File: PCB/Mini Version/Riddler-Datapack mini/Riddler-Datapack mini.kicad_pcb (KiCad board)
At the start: 4 copper layers, 50 x 68 mm, 57 parts, among them J1 UJ20-C-H-G-SMT-1-P16-TR, J2 DISPLAY, J4 Micro_SD_Card, SW1 RST, SW2 BOOT, U1 USBLC6-2P6, U2 ESP32-S3-MINI-1, U3 TLV62568DBV

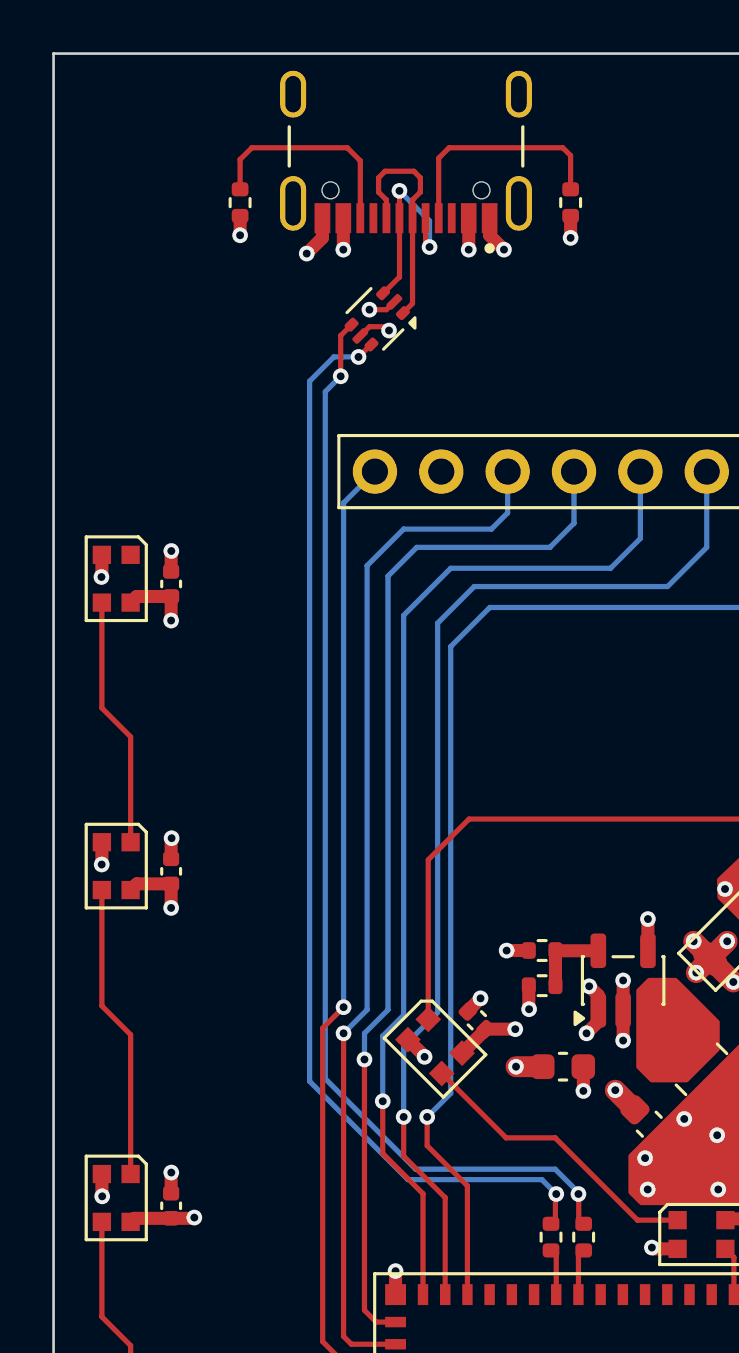
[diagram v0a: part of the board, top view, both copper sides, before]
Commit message: updated usbc location, added more relief vias to vbus and gnd
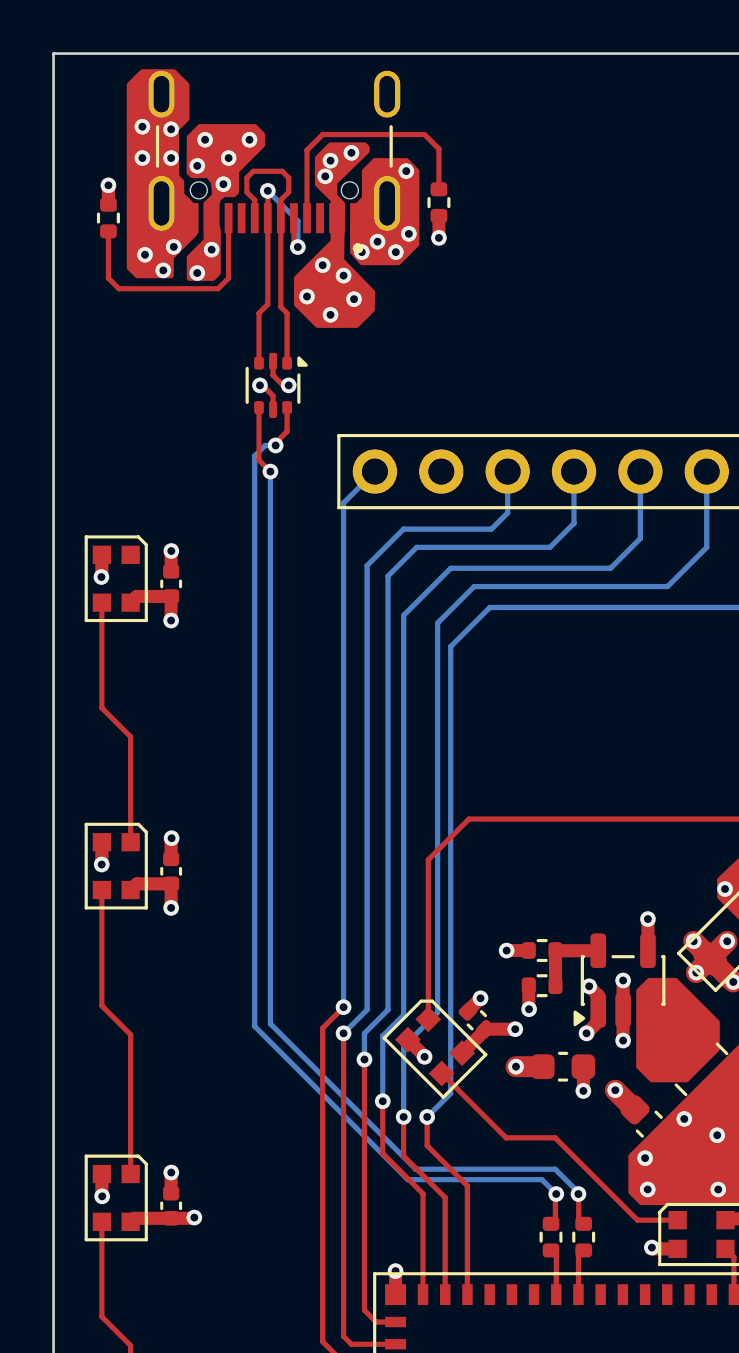
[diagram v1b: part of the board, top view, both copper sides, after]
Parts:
- moved R5 5.07 mm to (52.1, 36.3), turned to 90 degrees
- moved R4 5.04 mm to (64.8, 35.7)
- moved J1 5.04 mm to (58.5, 29.0)
- moved U1 4.73 mm to (58.4, 42.7), turned to -90 degrees
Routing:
- net GND: track 69.8 -> 67.0 mm, vias 70 -> 80
- net /Logic/D-: track 42.2 -> 39.5 mm
- net /Power/U_D-: track 7.97 -> 10.5 mm
- net VBUS: track 3.72 -> 1.19 mm, vias 11 -> 24
- net /Logic/D+: track 42.3 -> 40.0 mm
- net /Power/U_D+: track 8.93 -> 10.8 mm
- net /Power/CC1: track 8.92 -> 9.67 mm
- net /Power/CC2: track 8.33 -> 9.03 mm

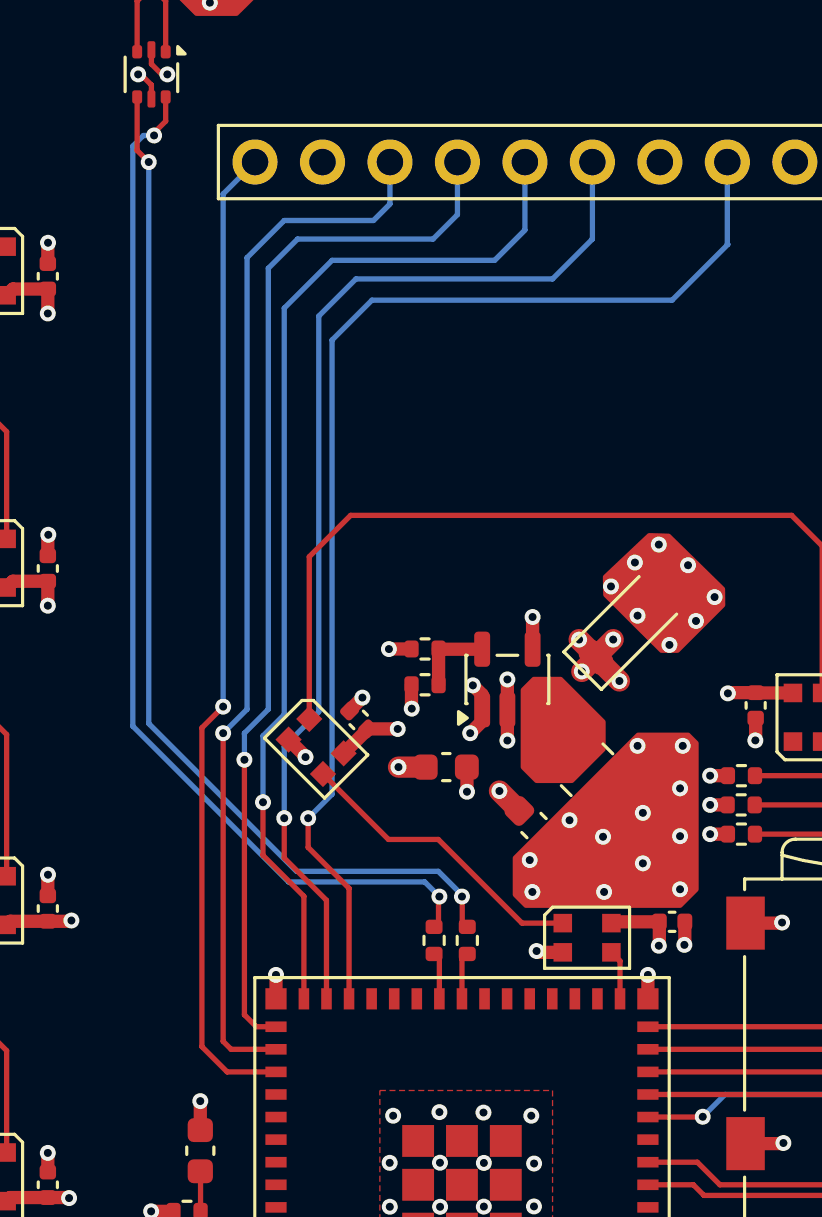
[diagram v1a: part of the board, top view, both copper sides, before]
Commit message: v1.1: update Mini Datapack with repositioned USB-C, relief vias, and v1p1 exports
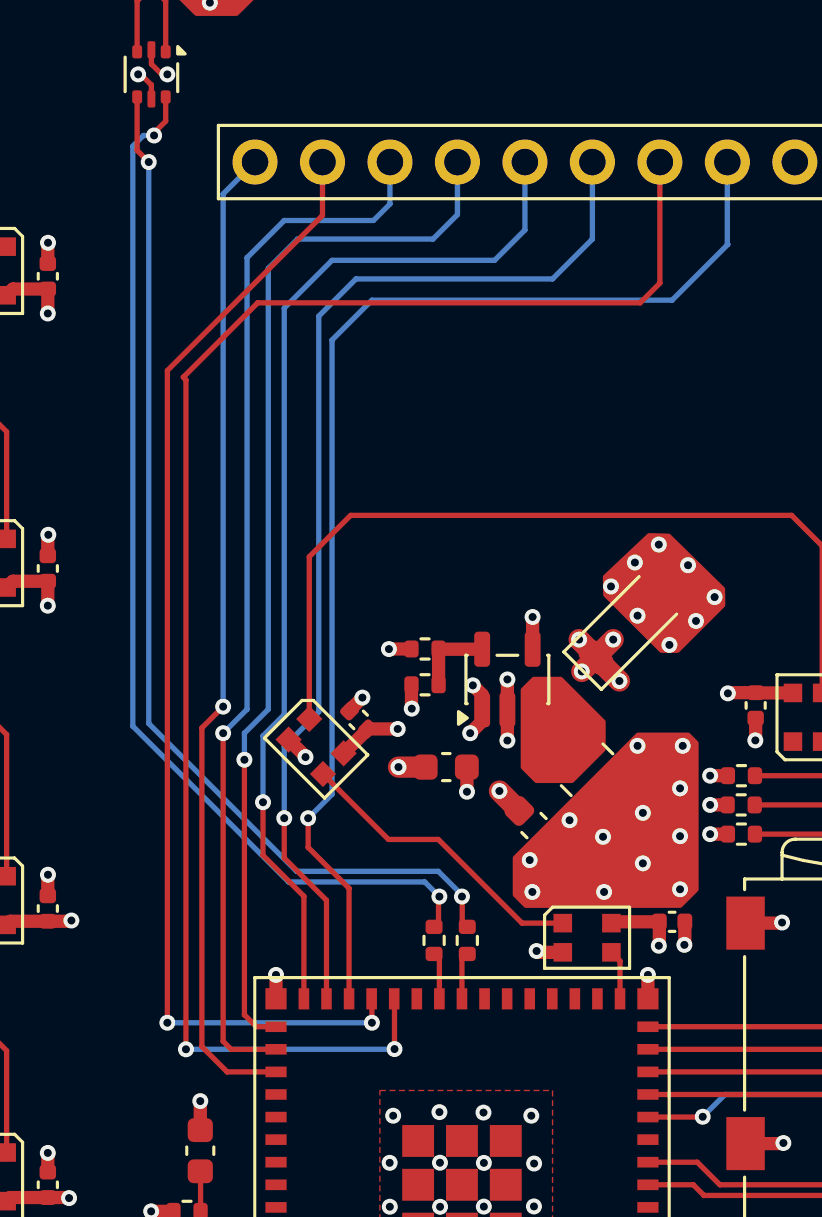
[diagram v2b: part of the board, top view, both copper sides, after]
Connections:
- J2 pad 10: unconnected-(J2-Pin_10-Pad10) -> /Logic/CS_SD2
- J2 pad 5: unconnected-(J2-Pin_5-Pad5) -> /Logic/MISO
- U2 pad 26: unconnected-(U2-IO26-Pad26) -> /Logic/MISO
- U2 pad 27: unconnected-(U2-IO47-Pad27) -> /Logic/CS_SD2
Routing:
- net /Logic/MISO: track 0.00 -> 59.1 mm, vias 0 -> 2
- net /Logic/CS_SD2: track 0.00 -> 43.4 mm, vias 0 -> 2

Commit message: production stuff and riddle me this text on pcb
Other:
- board text added: "RIDDLE ME THIS..."

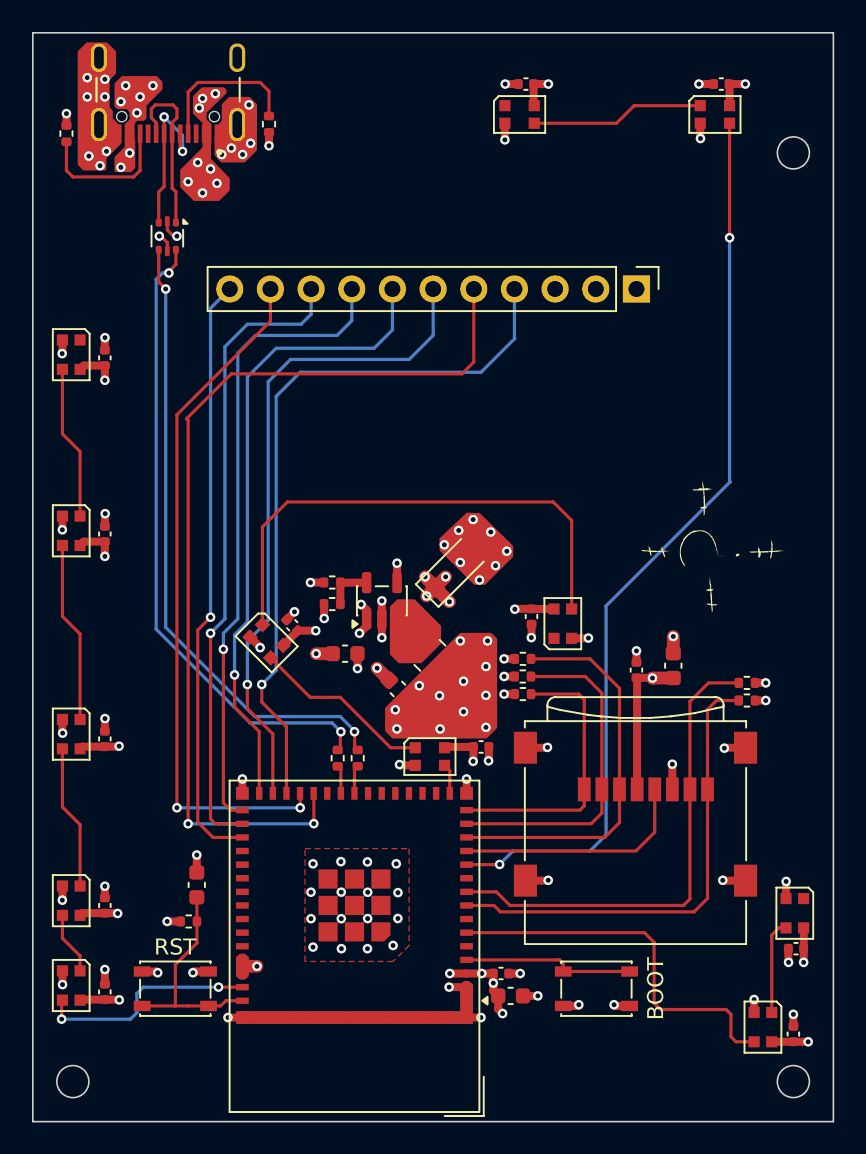
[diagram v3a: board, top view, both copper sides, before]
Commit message: feat(mini): release v1.2 - green solder mask, silkscreen polish, and JLCPCB production files
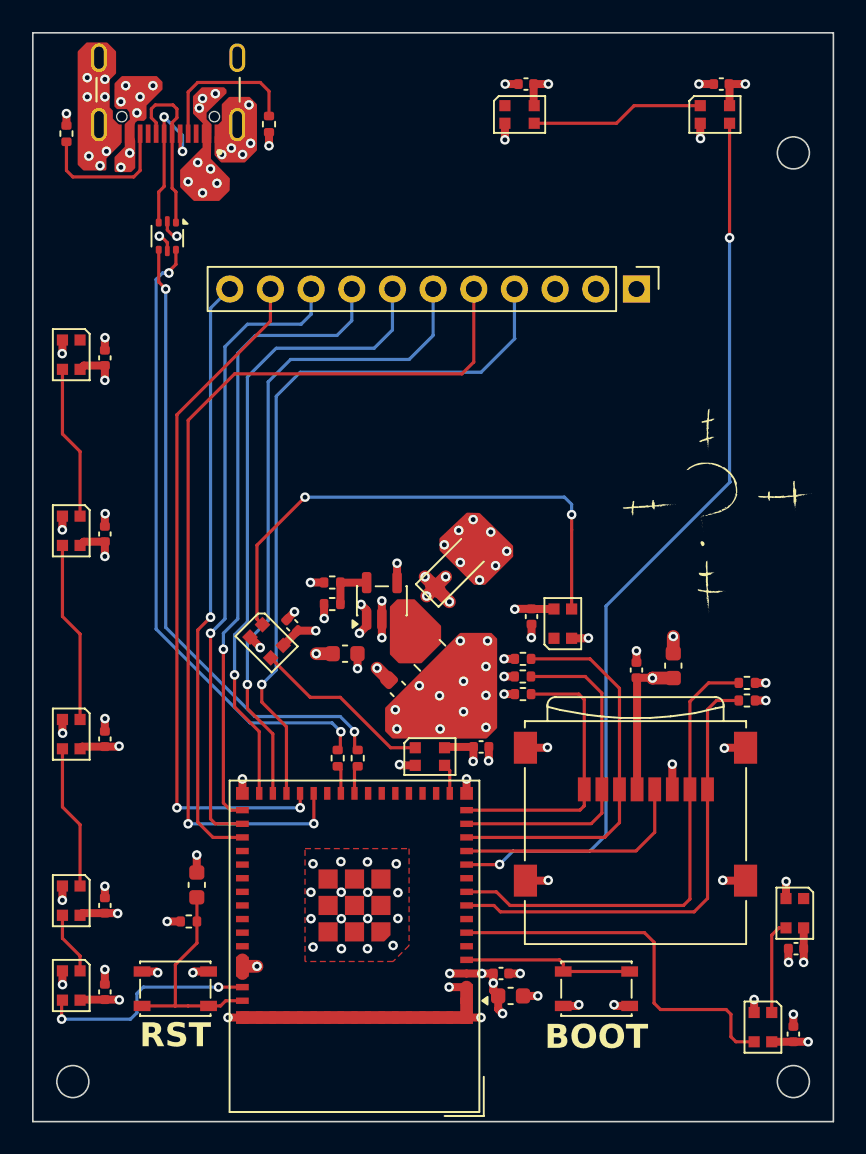
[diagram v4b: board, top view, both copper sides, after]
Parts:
- moved G*** 7.00 mm to (74.9, 65.8)
- moved G*** 6.48 mm to (86.5, 74.5)
- moved G*** 5.61 mm to (60.5, 70.1)
- moved G*** 1.41 mm to (93.1, 60.2), turned to 0 degrees
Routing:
- net Net-(D5-DOUT): track 32.1 -> 32.7 mm, vias 0 -> 2
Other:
- board text added: "A ROBIN ORIGINS ORIGINAL PROP"
